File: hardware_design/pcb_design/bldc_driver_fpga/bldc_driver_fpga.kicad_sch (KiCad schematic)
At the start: 33 parts, among them J1 Voltage Bus In, J2 Power, J3 Digital 1, J4 Digital 2, J5 Analog, J6 Motor Out, J7 Hall/Encoder

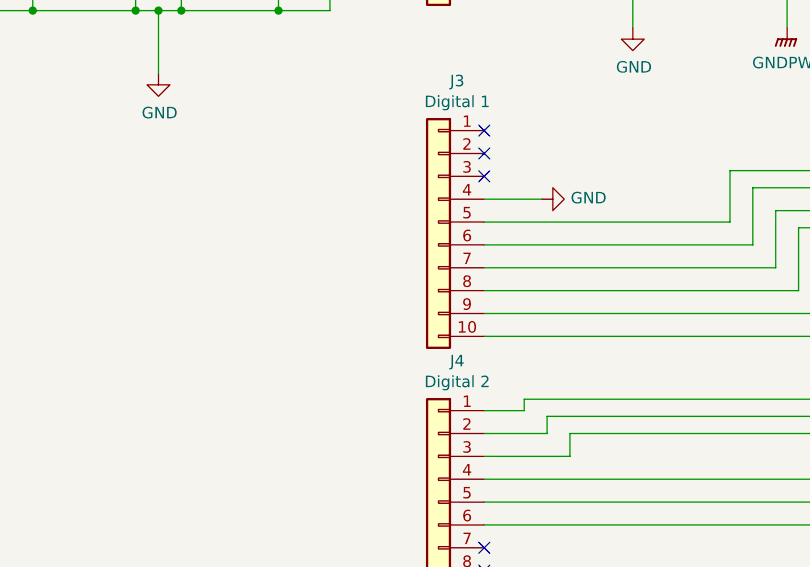
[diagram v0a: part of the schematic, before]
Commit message: Tested inverter, works. Tested ADC triggering, mostly works except not sure if current is correct. Found issue with back EMF causing FPGA to crash.
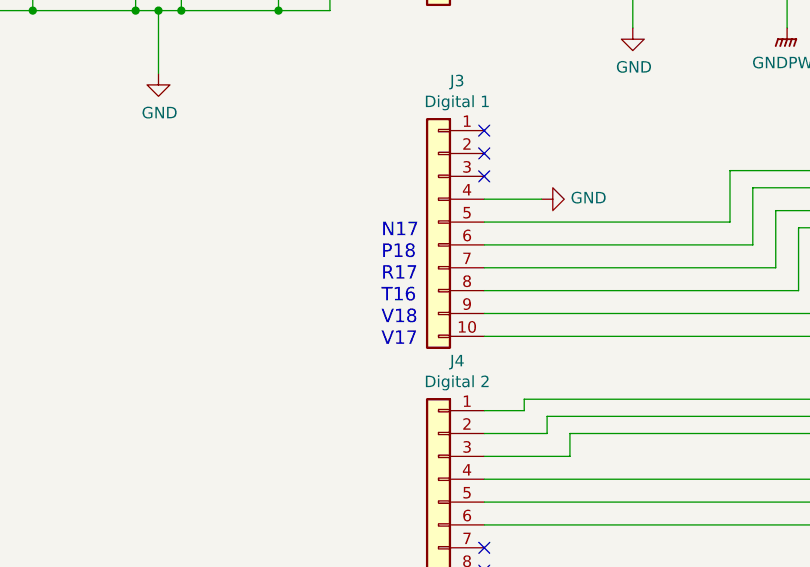
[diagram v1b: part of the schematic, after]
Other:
- note added: "N17 P18 R17 T16 V18 V17"
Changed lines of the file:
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@@
     (stroke (width 0) (type default) (color 0 0 0 0))
+  )
+  (text "N17\nP18\nR17\nT16\nV18\nV17" (at 63.5 104.14 0)
+    (effects (font (size 1.5 1.5)) (justify left bottom))
   )
   (text "CH6" (at 63.5 143.51 0)

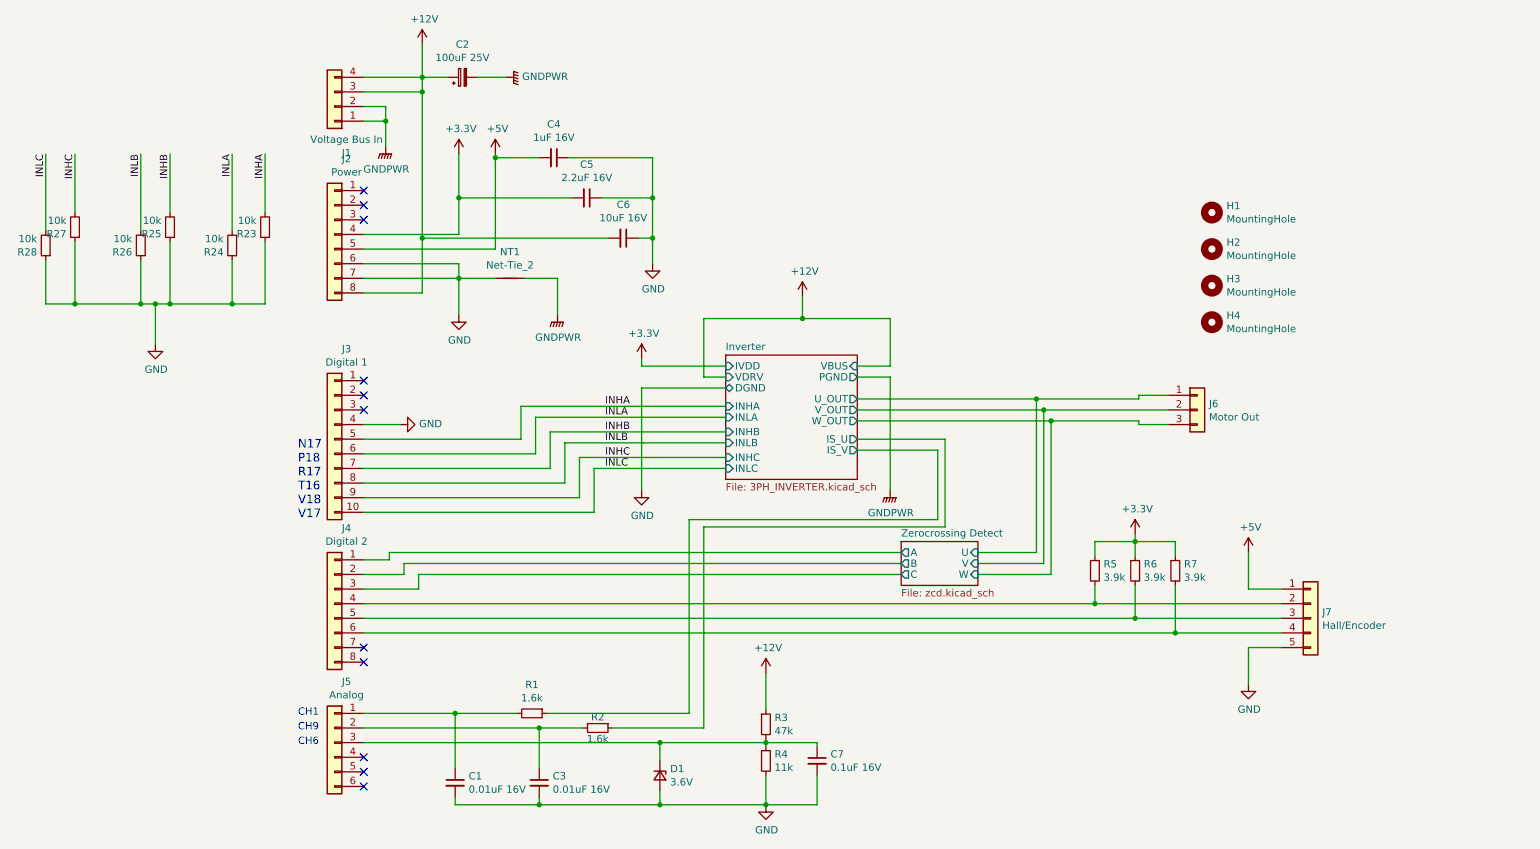
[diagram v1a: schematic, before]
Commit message: Implemented pure sinewave drive from programmable logic. Set up time base generator for ADC.
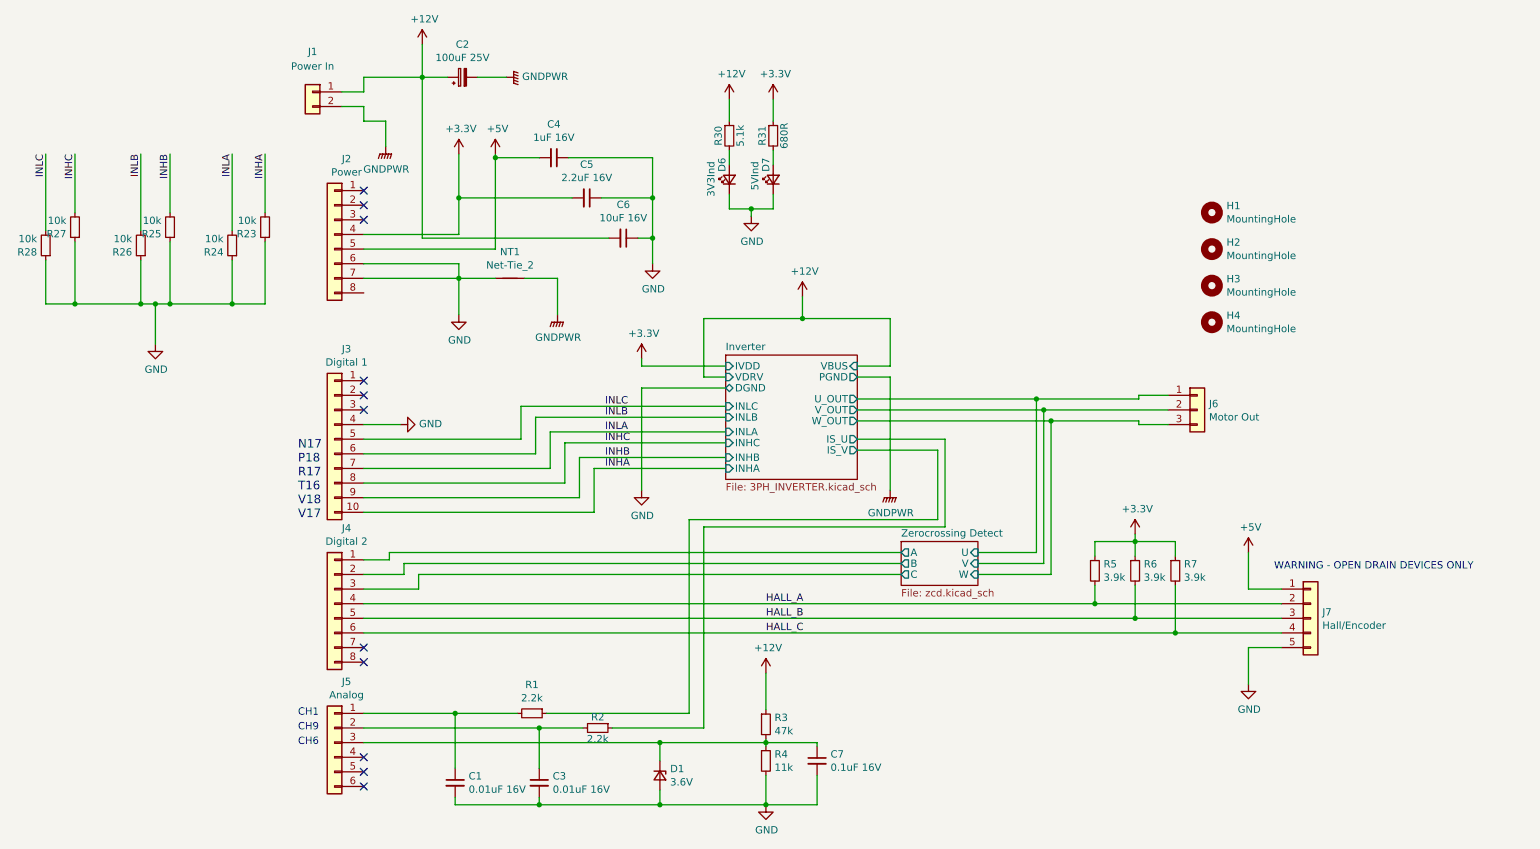
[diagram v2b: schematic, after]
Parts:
- removed J1: Voltage Bus In, Connector_Molex:Molex_Mini-Fit_Jr_5566-04A_2x02_P4.20mm_Vertical, symbol Connector_Generic:Conn_01x04
- added D6: 3V3Ind, LED_SMD:LED_0603_1608Metric_Pad1.05x0.95mm_HandSolder, symbol Device:LED_Small
- added D7: 5VInd, LED_SMD:LED_0603_1608Metric_Pad1.05x0.95mm_HandSolder, symbol Device:LED_Small
- added J1: Power In, Connector_JST:JST_PH_B2B-PH-K_1x02_P2.00mm_Vertical, symbol Connector_Generic:Conn_01x02
- added R30: 5.1k, Resistor_SMD:R_0603_1608Metric_Pad0.98x0.95mm_HandSolder, symbol Device:R_Small
- added R31: 680R, Resistor_SMD:R_0603_1608Metric_Pad0.98x0.95mm_HandSolder, symbol Device:R_Small
- C1, C3, C4, C5, C6, C7: footprint Capacitor_SMD:C_0603_1608Metric_Pad1.05x0.95mm_HandSolder -> Capacitor_SMD:C_0603_1608Metric_Pad1.08x0.95mm_HandSolder
- J6: footprint SamacSys_Parts:1054301103 -> Connector_JST:JST_PH_B3B-PH-K_1x03_P2.00mm_Vertical
- R1, R2: value 1.6k -> 2.2k
- R23, R24, R25, R26, R27, R28: footprint Resistor_SMD:R_0603_1608Metric_Pad1.05x0.95mm_HandSolder -> Resistor_SMD:R_0603_1608Metric_Pad0.98x0.95mm_HandSolder
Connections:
- net +12V: now also J1.1 (Pin_1), R30.1; no longer J2.8 (Pin_8)
- net +3V3: now also R31.1
- net GND: now also D6.1 (K), D7.1 (K)
- net GNDPWR: now also J1.2 (Pin_2)
- net INHA: now also J3.10 (Pin_10); no longer J3.5 (Pin_5)
- net INHB: now also J3.9 (Pin_9); no longer J3.7 (Pin_7)
- net INHC: now also J3.8 (Pin_8); no longer J3.9 (Pin_9)
- net INLA: now also J3.7 (Pin_7); no longer J3.6 (Pin_6)
- net INLB: now also J3.6 (Pin_6); no longer J3.8 (Pin_8)
- net INLC: now also J3.5 (Pin_5); no longer J3.10 (Pin_10)
- net HALL_A: now reaches J4.4 (Pin_4), J7.2 (Pin_2), R5.2
- net HALL_B: now reaches J4.5 (Pin_5), J7.3 (Pin_3), R6.2
- net HALL_C: now reaches J4.6 (Pin_6), J7.4 (Pin_4), R7.2
- new net: D7.2 (A), R31.2
- new net: D6.2 (A), R30.2
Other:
- note added: "WARNING - OPEN DRAIN DEVICES ONLY"
